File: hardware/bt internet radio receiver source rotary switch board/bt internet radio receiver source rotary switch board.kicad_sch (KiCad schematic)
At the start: 23 parts, among them J1 Conn_01x06_Pin, SW1 RS1010_1P5T

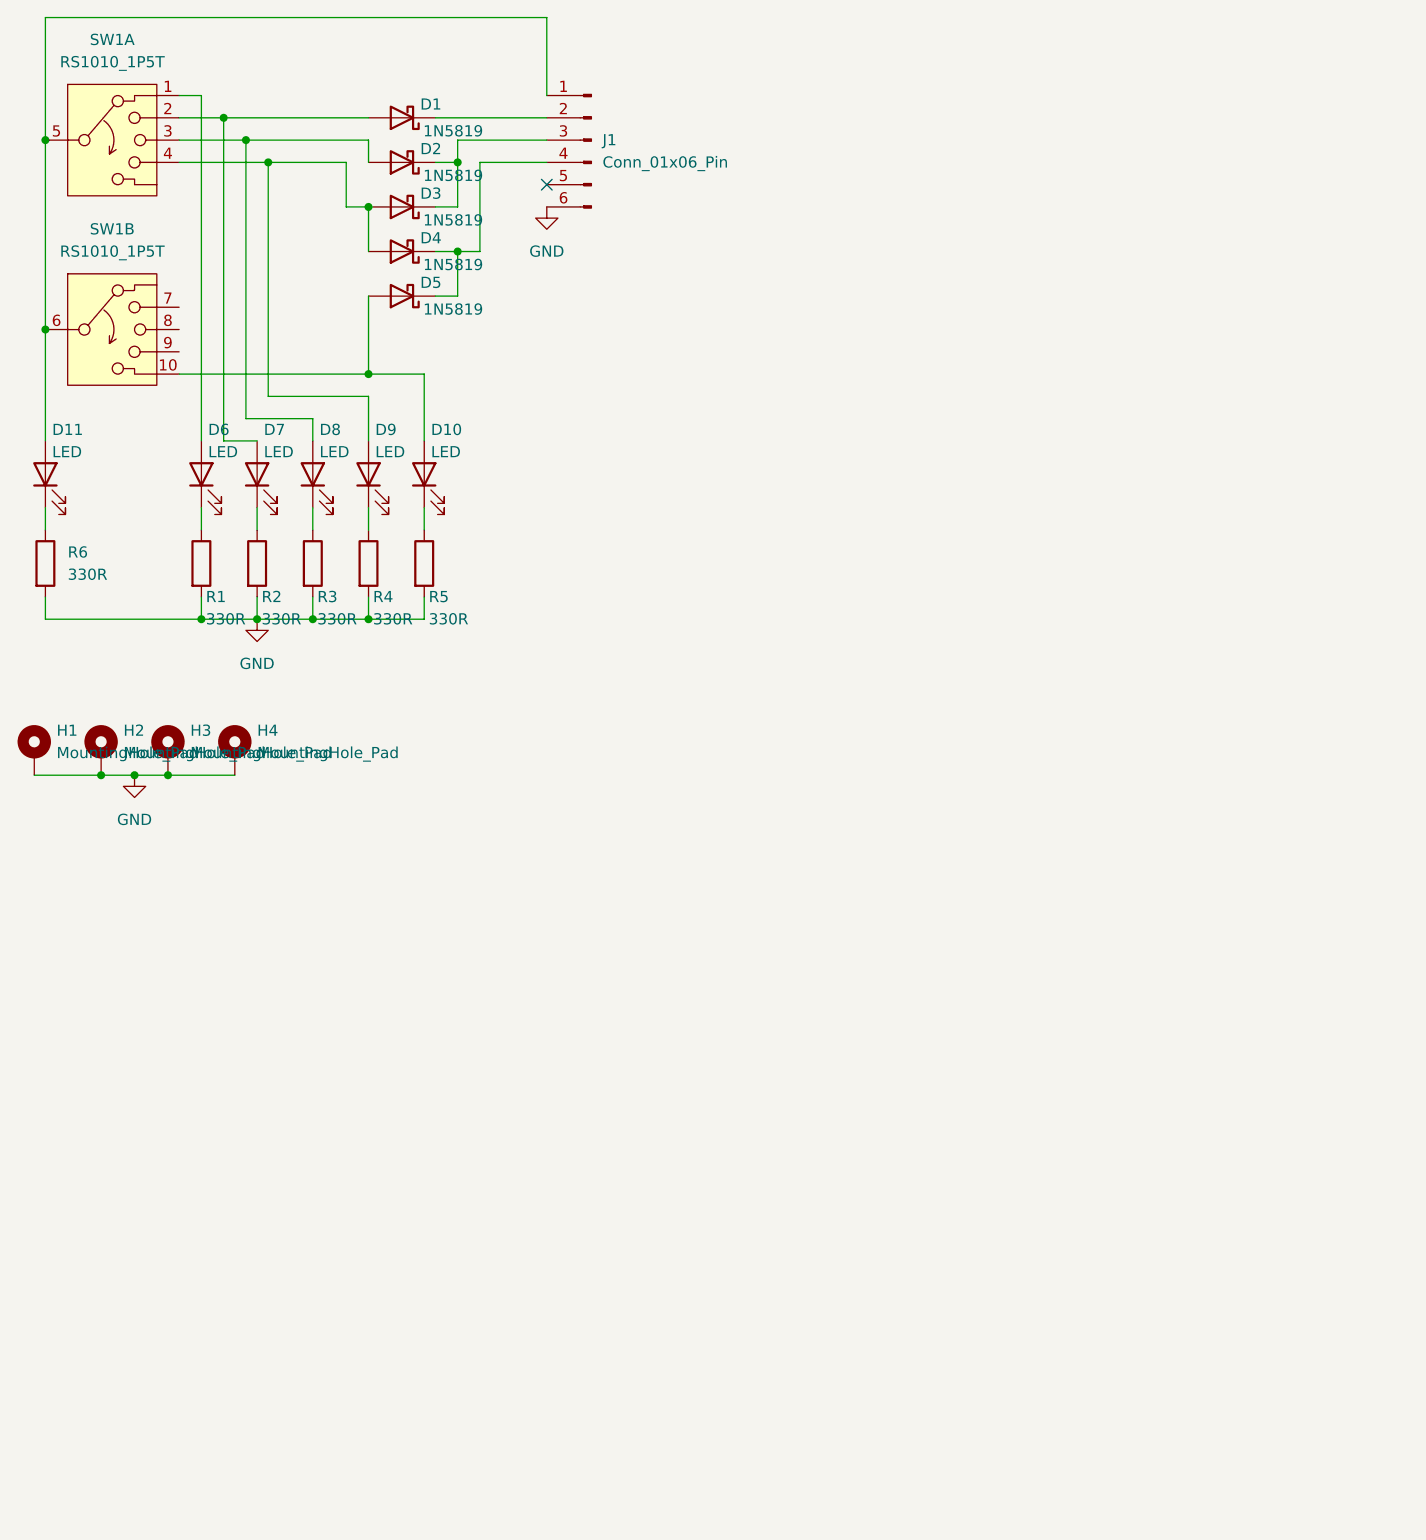
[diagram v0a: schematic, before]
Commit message: Cosmetic cleanup in schematics, add schematic PDF exports
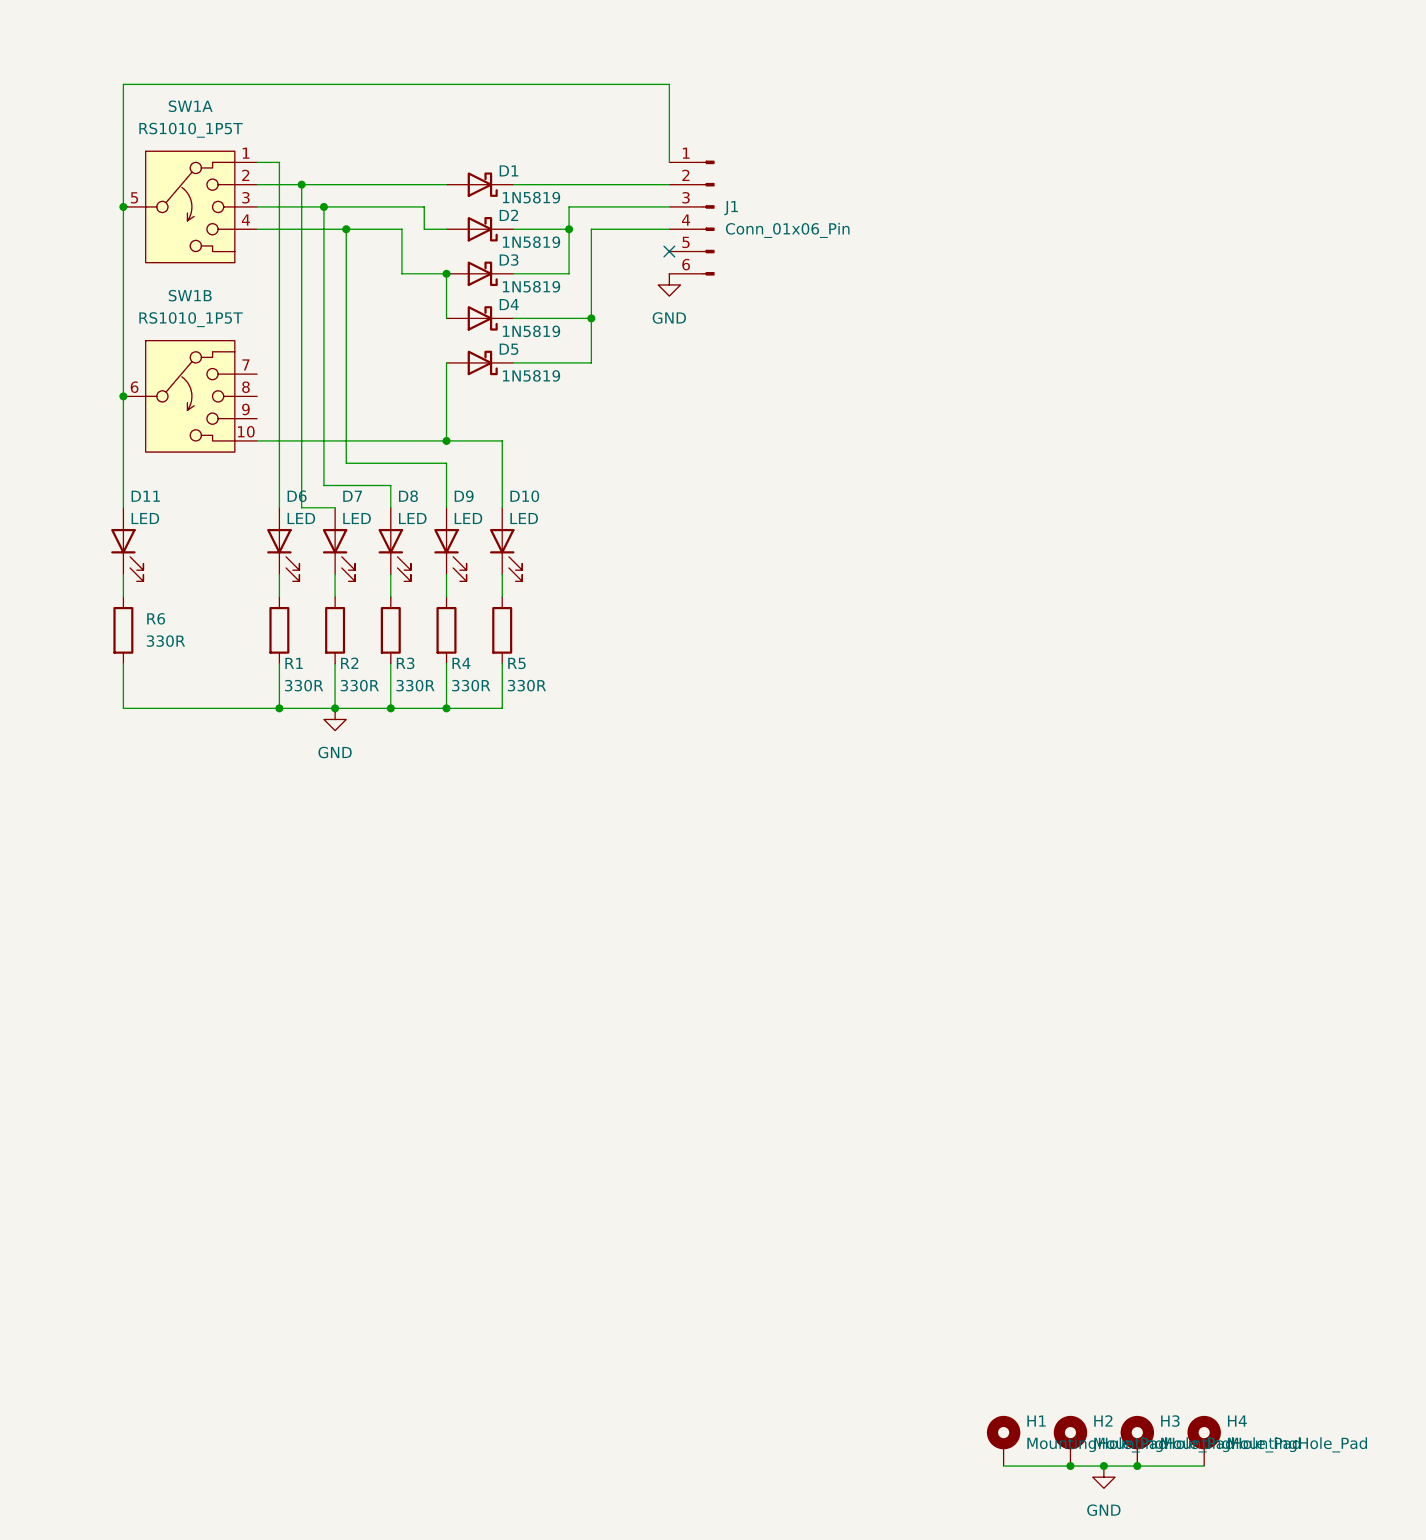
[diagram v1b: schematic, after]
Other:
- title: (none) -> Audiostreamer Rotary Switch Board
- moved on the sheet: D1, D10, D11, D2, D3, D4, D5, D6, D7, D8, D9, H1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
